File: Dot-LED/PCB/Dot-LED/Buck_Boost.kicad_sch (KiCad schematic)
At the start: 1 part, among them U3 TPS631000DRLR

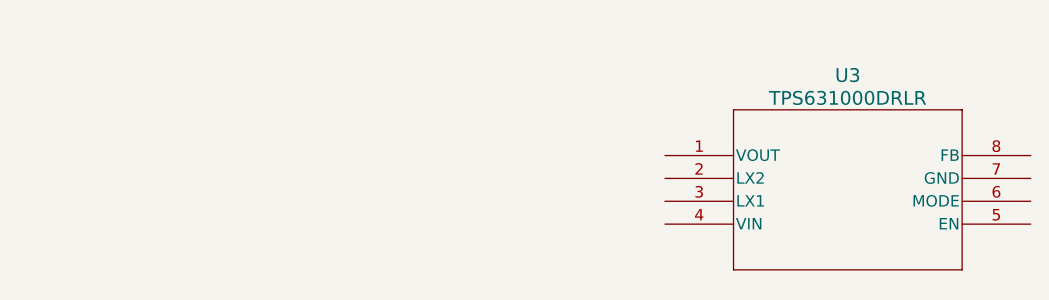
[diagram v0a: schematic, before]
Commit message: add common KiCad library using plugin
https://componentsearchengine.com/ga/downloads.php
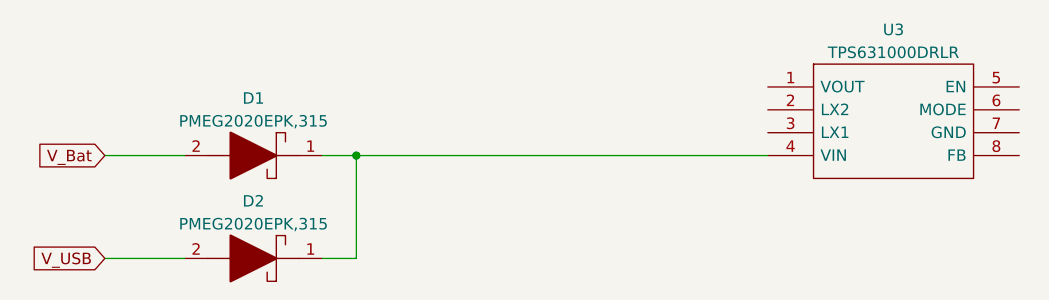
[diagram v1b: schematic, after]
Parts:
- removed U3: TPS631000DRLR, TI_Footprints:TPS631000DRLR_TEX, symbol TPS631000DRLR:TPS631000DRLR
- added D1, D2: PMEG2020EPK,315, PMEG2020EPK315, symbol SamacSys_Parts:PMEG2020EPK,315
- added U3: TPS631000DRLR, SOTFL50P160X60-8N, symbol SamacSys_Parts:TPS631000DRLR
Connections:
- new net: D1.1, D2.1, U3.4 (VIN)
- new net V_Bat: D1.2
- new net V_USB: D2.2
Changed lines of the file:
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@@
 (kicad_sch (version 20230121) (generator eeschema)
   (paper "A4")
-  (symbol (lib_id "TPS631000DRLR:TPS631000DRLR") (at 130.81 74.93 0) (unit 1)
+  (junction (at 96.52 74.93) (diameter 0) (color 0 0 0 0)
+  )
+  (wire (pts (xy 96.52 86.36) (xy 92.71 86.36))
+    (stroke (width 0) (type default))
+  )
+  (wire (pts (xy 68.58 86.36) (xy 77.47 86.36))
+    (stroke (width 0) (type default))
+  )
+  (wire (pts (xy 68.58 74.93) (xy 77.47 74.93))
+    (stroke (width 0) (type default))
+  )
+  (wire (pts (xy 96.52 74.93) (xy 142.24 74.93))
+    (stroke (width 0) (type default))
+  )
+  (wire (pts (xy 96.52 74.93) (xy 96.52 86.36))
+    (stroke (width 0) (type default))
+  )
+  (wire (pts (xy 92.71 74.93) (xy 96.52 74.93))
+    (stroke (width 0) (type default))
+  )
+  (global_label "V_Bat" (shape input) (at 68.58 74.93 180) (fields_autoplaced)
+    (effects (font (size 1.27 1.27)) (justify right))
+    (property "Intersheetrefs" "${INTERSHEET_REFS}" (at 60.4733 74.93 0)
+      (effects (font (size 1.27 1.27)) (justify right) hide)
+    )
+  )
+  (global_label "V_USB" (shape input) (at 68.58 86.36 180) (fields_autoplaced)
+    (effects (font (size 1.27 1.27)) (justify right))
+    (property "Intersheetrefs" "${INTERSHEET_REFS}" (at 59.808 86.36 0)
+      (effects (font (size 1.27 1.27)) (justify right) hide)
+    )
+  )
+  (symbol (lib_id "SamacSys_Parts:PMEG2020EPK,315") (at 95.25 86.36 180) (unit 1)
     (in_bom yes) (on_board yes) (dnp no) (fields_autoplaced)
-    (property "Reference" "U3" (at 151.13 66.04 0)
-      (effects (font (size 1.524 1.524)))
+    (property "Reference" "D2" (at 85.09 80.01 0)
+      (effects (font (size 1.27 1.27)))
     )
-    (property "Value" "TPS631000DRLR" (at 151.13 68.58 0)
-      (effects (font (size 1.524 1.524)))
+    (property "Value" "PMEG2020EPK,315" (at 85.09 82.55 0)
+      (effects (font (size 1.27 1.27)))
     )
-    (property "Footprint" "TI_Footprints:TPS631000DRLR_TEX" (at 130.81 74.93 0)
-      (effects (font (size 1.27 1.27) italic) hide)
+    (property "Footprint" "PMEG2020EPK315" (at 82.55 90.17 0)
+      (effects (font (size 1.27 1.27)) (justify left) hide)
     )
-    (property "Datasheet" "TPS631000DRLR" (at 130.81 74.93 0)
-      (effects (font (size 1.27 1.27) italic) hide)
+    (property "Datasheet" "https://assets.nexperia.com/documents/data-sheet/PMEG2020EPK.pdf" (at 82.55 87.63 0)
+      (effects (font (size 1.27 1.27)) (justify left) hide)
+    )
+    (property "Description" "NEXPERIA - PMEG2020EPK,315 - Schottky Rectifier, 20 V, 2 A, Single, SOD-1608, 2 Pins, 450 mV" (at 82.55 85.09 0)
+      (effects (font (size 1.27 1.27)) (justify left) hide)
+    )
+    (property "Height" "0.4" (at 82.55 82.55 0)
+      (effects (font (size 1.27 1.27)) (justify left) hide)
+    )
+    (property "Manufacturer_Name" "Nexperia" (at 82.55 80.01 0)
+      (effects (font (size 1.27 1.27)) (justify left) hide)
+    )
+    (property "Manufacturer_Part_Number" "PMEG2020EPK,315" (at 82.55 77.47 0)
+      (effects (font (size 1.27 1.27)) (justify left) hide)
+    )
+    (property "Mouser Part Number" "771-PMEG2020EPK,315" (at 82.55 74.93 0)
+      (effects (font (size 1.27 1.27)) (justify left) hide)
+    )
+    (property "Mouser Price/Stock" "https://www.mouser.co.uk/ProductDetail/Nexperia/PMEG2020EPK315?qs=zHGtguZFFhKxs4HM5hK1uw%3D%3D" (at 82.55 72.39 0)
+      (effects (font (size 1.27 1.27)) (justify left) hide)
+    )
+    (property "Arrow Part Number" "PMEG2020EPK,315" (at 82.55 69.85 0)
+      (effects (font (size 1.27 1.27)) (justify left) hide)
+    )
+    (property "Arrow Price/Stock" "https://www.arrow.com/en/products/pmeg2020epk315/nexperia?region=nac" (at 82.55 67.31 0)
+      (effects (font (size 1.27 1.27)) (justify left) hide)
+    )
+    (pin "1")
+    (pin "2")
+    (instances
+      (project "Dot-LED"
+        (path "/e63e39d7-6ac0-4ffd-8aa3-1841a4541b55/eadb16b8-295e-4810-8d56-9eb69942c69b"
+          (reference "D2") (unit 1)
+        )
+      )
+    )
+  )
+  (symbol (lib_id "SamacSys_Parts:TPS631000DRLR") (at 142.24 67.31 0) (unit 1)
+    (in_bom yes) (on_board yes) (dnp no) (fields_autoplaced)
+    (property "Reference" "U3" (at 156.21 60.96 0)
+      (effects (font (size 1.27 1.27)))
+    )
+    (property "Value" "TPS631000DRLR" (at 156.21 63.5 0)
+      (effects (font (size 1.27 1.27)))
+    )
+    (property "Footprint" "SOTFL50P160X60-8N" (at 166.37 64.77 0)
+      (effects (font (size 1.27 1.27)) (justify left) hide)
+    )
+    (property "Datasheet" "https://www.ti.com/lit/ds/symlink/tps631000.pdf?ts=1652152702265" (at 166.37 67.31 0)
+      (effects (font (size 1.27 1.27)) (justify left) hide)
+    )
+    (property "Description" "Switching Voltage Regulators 1.5-A output current, high power density buck-boost converter" (at 166.37 69.85 0)
+      (effects (font (size 1.27 1.27)) (justify left) hide)
+    )
+    (property "Height" "0.6" (at 166.37 72.39 0)
+      (effects (font (size 1.27 1.27)) (justify left) hide)
+    )
+    (property "Manufacturer_Name" "Texas Instruments" (at 166.37 74.93 0)
+      (effects (font (size 1.27 1.27)) (justify left) hide)
+    )
+    (property "Manufacturer_Part_Number" "TPS631000DRLR" (at 166.37 77.47 0)
+      (effects (font (size 1.27 1.27)) (justify left) hide)
+    )
+    (property "Mouser Part Number" "595-TPS631000DRLR" (at 166.37 80.01 0)
+      (effects (font (size 1.27 1.27)) (justify left) hide)
+    )
+    (property "Mouser Price/Stock" "https://www.mouser.co.uk/ProductDetail/Texas-Instruments/TPS631000DRLR?qs=rSMjJ%252B1ewcRYwoN2deTeNA%3D%3D" (at 166.37 82.55 0)
+      (effects (font (size 1.27 1.27)) (justify left) hide)
+    )
+    (property "Arrow Part Number" "TPS631000DRLR" (at 166.37 85.09 0)
+      (effects (font (size 1.27 1.27)) (justify left) hide)
+    )
+    (property "Arrow Price/Stock" "https://www.arrow.com/en/products/tps631000drlr/texas-instruments?region=nac" (at 166.37 87.63 0)
+      (effects (font (size 1.27 1.27)) (justify left) hide)
     )
     (pin "1")
@@
         )
       )
+    )
+  )
+  (symbol (lib_id "SamacSys_Parts:PMEG2020EPK,315") (at 95.25 74.93 180) (unit 1)
+    (in_bom yes) (on_board yes) (dnp no) (fields_autoplaced)
+    (property "Reference" "D1" (at 85.09 68.58 0)
+      (effects (font (size 1.27 1.27)))
+    )
+    (property "Value" "PMEG2020EPK,315" (at 85.09 71.12 0)
+      (effects (font (size 1.27 1.27)))
+    )
+    (property "Footprint" "PMEG2020EPK315" (at 82.55 78.74 0)
+      (effects (font (size 1.27 1.27)) (justify left) hide)
+    )
+    (property "Datasheet" "https://assets.nexperia.com/documents/data-sheet/PMEG2020EPK.pdf" (at 82.55 76.2 0)
+      (effects (font (size 1.27 1.27)) (justify left) hide)
+    )
+    (property "Description" "NEXPERIA - PMEG2020EPK,315 - Schottky Rectifier, 20 V, 2 A, Single, SOD-1608, 2 Pins, 450 mV" (at 82.55 73.66 0)
+      (effects (font (size 1.27 1.27)) (justify left) hide)
+    )
+    (property "Height" "0.4" (at 82.55 71.12 0)
+      (effects (font (size 1.27 1.27)) (justify left) hide)
+    )
+    (property "Manufacturer_Name" "Nexperia" (at 82.55 68.58 0)
+      (effects (font (size 1.27 1.27)) (justify left) hide)
+    )
+    (property "Manufacturer_Part_Number" "PMEG2020EPK,315" (at 82.55 66.04 0)
+      (effects (font (size 1.27 1.27)) (justify left) hide)
+    )
+    (property "Mouser Part Number" "771-PMEG2020EPK,315" (at 82.55 63.5 0)
+      (effects (font (size 1.27 1.27)) (justify left) hide)
+    )
+    (property "Mouser Price/Stock" "https://www.mouser.co.uk/ProductDetail/Nexperia/PMEG2020EPK315?qs=zHGtguZFFhKxs4HM5hK1uw%3D%3D" (at 82.55 60.96 0)
+      (effects (font (size 1.27 1.27)) (justify left) hide)
+    )
+    (property "Arrow Part Number" "PMEG2020EPK,315" (at 82.55 58.42 0)
+      (effects (font (size 1.27 1.27)) (justify left) hide)
+    )
+    (property "Arrow Price/Stock" "https://www.arrow.com/en/products/pmeg2020epk315/nexperia?region=nac" (at 82.55 55.88 0)
+      (effects (font (size 1.27 1.27)) (justify left) hide)
+    )
+    (pin "1")
+    (pin "2")
+    (instances
+      (project "Dot-LED"
+        (path "/e63e39d7-6ac0-4ffd-8aa3-1841a4541b55/eadb16b8-295e-4810-8d56-9eb69942c69b"
+          (reference "D1") (unit 1)
+        )
+      )

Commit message: Update DotLED Schem
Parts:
- added C3 (x3): 10uf, Capacitor_SMD:C_0603_1608Metric_Pad1.08x0.95mm_HandSolder, symbol SamacSys_Parts:0402B102K500NT
- added C3 (x2): 1uF, Capacitor_SMD:C_0603_1608Metric_Pad1.08x0.95mm_HandSolder, symbol SamacSys_Parts:0402B102K500NT
- added C4 (x2): 100nf, Capacitor_SMD:C_0603_1608Metric_Pad1.08x0.95mm_HandSolder, symbol SamacSys_Parts:0402B102K500NT
- added L2: DFE252012PD-1R0M=P2, DFE2HCAH1R0MJ0L, symbol SamacSys_Parts:DFE252012PD-1R0M=P2
- added R3 (x2): 15k, RESC1608X55N, symbol SamacSys_Parts:RMCF0603ZT0R00
- added R5: 91k, RESC1608X55N, symbol SamacSys_Parts:RMCF0603ZT0R00
- added R5: 511k, RESC1608X55N, symbol SamacSys_Parts:RMCF0603ZT0R00
- D1, D2: Digi-Key_PN (none) -> 771-PMEG2020EPK,315
- U3: Digi-Key_PN (none) -> 595-TPS631000DRLR
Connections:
- net VIN: now reaches D1.1, D2.1, U3.4 (VIN)
- net VIN: now also C3.2, C3.2, C4.2, R3.2, R3.2
- net 3V3_VCC: now reaches U3.1 (VOUT)
- net 3V3_VCC: now also C3.1, C3.1, C3.1, C4.1, R5.1
- net at U3.2 (LX2): now also L2.2
- net at U3.3 (LX1): now also L2.1
- net at U3.5 (EN): now also R3.1
- net at U3.6 (MODE): now also R3.1
- net GND: now reaches U3.7 (GND)
- net GND: now also C3.1, C3.1, C3.2, C3.2, C3.2, C4.1, C4.2, R5.2
- net at U3.8 (FB): now also R5.1, R5.2

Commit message: Update Vreg to in-stock component
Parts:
- added IC1: TPS631010YBGR, BGA8C40P2X4_86X176X50, symbol SamacSys_Parts:TPS631010YBGR
- C3: LCSC Part Number (none) -> C96446
- C3: LCSC Part Number (none) -> C15849
- C4: LCSC Part Number (none) -> C14663
- D1, D2: LCSC Part Number (none) -> C552841
- L2: LCSC Part Number (none) -> C285917
- R3: LCSC Part Number (none) -> C22809
- R5: LCSC Part Number (none) -> C101235
- R5: LCSC Part Number (none) -> C3016414
- U3: LCSC Part Number (none) -> C5219190
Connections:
- net 3V3_VCC: no longer U3.1 (VOUT)
- net GND: now also IC1.C2 (GND); no longer U3.7 (GND)
- net VIN: now also IC1.A1 (VIN); no longer U3.4 (VIN)
- net at U3.2 (LX2): no longer L2.2
- net at U3.3 (LX1): no longer L2.1
- net at U3.5 (EN): no longer R3.1
- net at U3.6 (MODE): no longer R3.1
- net at R5.1, R5.2: no longer U3.8 (FB)
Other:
- moved on the sheet: U3

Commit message: small change to schem for new vreg
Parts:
- removed L2: DFE252012PD-1R0M=P2, DFE2HCAH1R0MJ0L, symbol SamacSys_Parts:DFE252012PD-1R0M=P2
- removed R3 (x2): 15k, RESC1608X55N, symbol SamacSys_Parts:RMCF0603ZT0R00
- removed U3: TPS631000DRLR, SOTFL50P160X60-8N, symbol SamacSys_Parts:TPS631000DRLR
- added L1: DFE252012PD-1R0M=P2, DFE2HCAH1R0MJ0L, symbol SamacSys_Parts:DFE252012PD-1R0M=P2
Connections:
- net 3V3_VCC is gone; now on net SW: C3.1, C3.1, C3.1, C4.1, R5.1
- net GND: now also IC1.B2 (MODE)
- net VIN: now also IC1.A2 (EN)
- net at R5.1, R5.2: now also IC1.D2 (FB)
- net L1: now reaches IC1.B1 (LX1)
- net L1: now also L1.1
- net at IC1.C1 (LX2): now also L1.2
- net SW: now reaches IC1.D1 (VOUT)

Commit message: finalize design based on in-stock parts
Gerber out 1.0
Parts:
- C3: MPN (none) -> C96446
- C3: MPN (none) -> C15849
- C4: MPN (none) -> C14663
- D1, D2: MPN (none) -> C552841
- IC1: LCSC Part Number (none) -> C6719123; MPN (none) -> C6719123
- L1: MPN (none) -> C285917
- R5: MPN (none) -> C101235
- R5: MPN (none) -> C3016414
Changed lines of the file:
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@@
+      (effects (font (size 1.27 1.27)) hide)
+    )
+    (property "MPN" "C552841" (at 95.25 86.36 0)
       (effects (font (size 1.27 1.27)) hide)
     )
@@
     )
     (property "LCSC Part Number" "C14663" (at 128.27 87.63 0)
+      (effects (font (size 1.27 1.27)) hide)
+    )
+    (property "MPN" "C14663" (at 128.27 87.63 0)
       (effects (font (size 1.27 1.27)) hide)
     )
@@
     )
     (property "LCSC Part Number" "C96446" (at 151.13 57.15 0)
+      (effects (font (size 1.27 1.27)) hide)
+    )
+    (property "MPN" "C96446" (at 151.13 57.15 0)
       (effects (font (size 1.27 1.27)) hide)
     )
@@
       (effects (font (size 1.27 1.27)) hide)
     )
+    (property "MPN" "C101235" (at 193.04 77.47 0)
+      (effects (font (size 1.27 1.27)) hide)
+    )
     (pin "1")
     (pin "2")
@@
     (property "Arrow Price/Stock" "https://www.arrow.com/en/products/tps631010ybgr/texas-instruments?region=nac" (at 166.37 92.71 0)
       (effects (font (size 1.27 1.27)) (justify left) hide)
+    )
+    (property "LCSC Part Number" "C6719123" (at 142.24 72.39 0)
+      (effects (font (size 1.27 1.27)) hide)
+    )
+    (property "MPN" "C6719123" (at 142.24 72.39 0)
+      (effects (font (size 1.27 1.27)) hide)
     )
     (pin "A1")
@@
       (effects (font (size 1.27 1.27)) hide)
     )
+    (property "MPN" "C15849" (at 118.11 87.63 0)
+      (effects (font (size 1.27 1.27)) hide)
+    )
     (pin "1")
     (pin "2")
@@
       (effects (font (size 1.27 1.27)) hide)
     )
+    (property "MPN" "C96446" (at 106.68 87.63 0)
+      (effects (font (size 1.27 1.27)) hide)
+    )
     (pin "1")
     (pin "2")
@@
       (effects (font (size 1.27 1.27)) hide)
     )
+    (property "MPN" "C14663" (at 172.72 57.15 0)
+      (effects (font (size 1.27 1.27)) hide)
+    )
     (pin "1")
     (pin "2")
@@
       (effects (font (size 1.27 1.27)) hide)
     )
+    (property "MPN" "C15849" (at 162.56 57.15 0)
+      (effects (font (size 1.27 1.27)) hide)
+    )
     (pin "1")
     (pin "2")
@@
     )
     (property "LCSC Part Number" "C285917" (at 146.05 63.5 0)
+      (effects (font (size 1.27 1.27)) hide)
+    )
+    (property "MPN" "C285917" (at 146.05 63.5 0)
       (effects (font (size 1.27 1.27)) hide)
     )
@@
       (effects (font (size 1.27 1.27)) hide)
     )
+    (property "MPN" "C3016414" (at 193.04 57.15 0)
+      (effects (font (size 1.27 1.27)) hide)
+    )
     (pin "1")
     (pin "2")
@@
       (effects (font (size 1.27 1.27)) hide)
     )
+    (property "MPN" "C552841" (at 95.25 74.93 0)
+      (effects (font (size 1.27 1.27)) hide)
+    )
     (pin "1")
     (pin "2")
@@
       (effects (font (size 1.27 1.27)) hide)
     )
+    (property "MPN" "C96446" (at 185.42 57.15 0)
+      (effects (font (size 1.27 1.27)) hide)
+    )
